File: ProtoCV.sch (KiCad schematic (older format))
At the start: 142 parts, among them J1 AudioJack2_SwitchT, J10 Conn_01x01_Male, J11 Conn_01x05_Male, J12 Conn_01x09_Male, J13 AudioJack2_SwitchT, J14 AudioJack2_SwitchT, J15 AudioJack2_SwitchT, J16 AudioJack2_SwitchT, J17 AudioJack2_SwitchT, J18 AudioJack2_SwitchT, J19 AudioJack2_SwitchT, J2 AudioJack2_SwitchT, J20 AudioJack2_SwitchT, J21 Conn_01x01_Male, J22 Conn_01x01_Male, J23 Conn_01x01_Male, J24 Conn_01x01_Male, J25 Conn_01x01_Male, J26 Conn_01x01_Male, J27 Conn_01x01_Male, J28 Conn_01x01_Male, J29 Conn_01x01_Male, J3 AudioJack2_SwitchT, J30 Conn_01x01_Male, J4 AudioJack2_SwitchT, J5 AudioJack2_SwitchT, J6 AudioJack2_SwitchT, J7 AudioJack2_SwitchT, J8 AudioJack2_SwitchT, J9 Conn_02x05_Odd_Even, Q1 BC847, Q2 BC847, Q3 BC847, Q4 BC847, Q5 BC847, Q6 BC847, Q7 BC847, Q8 BC847, U1 OPA4192, U2 OPA4192, U3 ADC80508Z, U4 R-78E3.3-0.5, U5 LD2981ABU33TR, U6 74AHCT244, U7 L7805

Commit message: Lots of manual routing.
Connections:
- net CV1: now also R12.1, R8.1; no longer R10.1, R6.1
- net CV2: now also R17.1, R21.1; no longer R11.1, R7.1
- net CV3: now also R20.1, R24.1; no longer R12.1, R8.1
- net CV4: now also R19.1, R23.1; no longer R17.1, R21.1
- net CV6: now also R11.1, R7.1; no longer R19.1, R23.1
- net CV7: now also R10.1, R6.1; no longer R20.1, R24.1
- net OUT1: now also R4.2; no longer R2.2
- net OUT2: now also R13.2; no longer R3.2
- net OUT3: now also R16.2; no longer R4.2
- net OUT4: now also R15.2; no longer R13.2
- net OUT6: now also R3.2; no longer R15.2
- net OUT7: now also R2.2; no longer R16.2
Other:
- moved on the sheet: C10, C2, C3, C4, C7, C9, R10, R11, R12, R13, R15, R16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

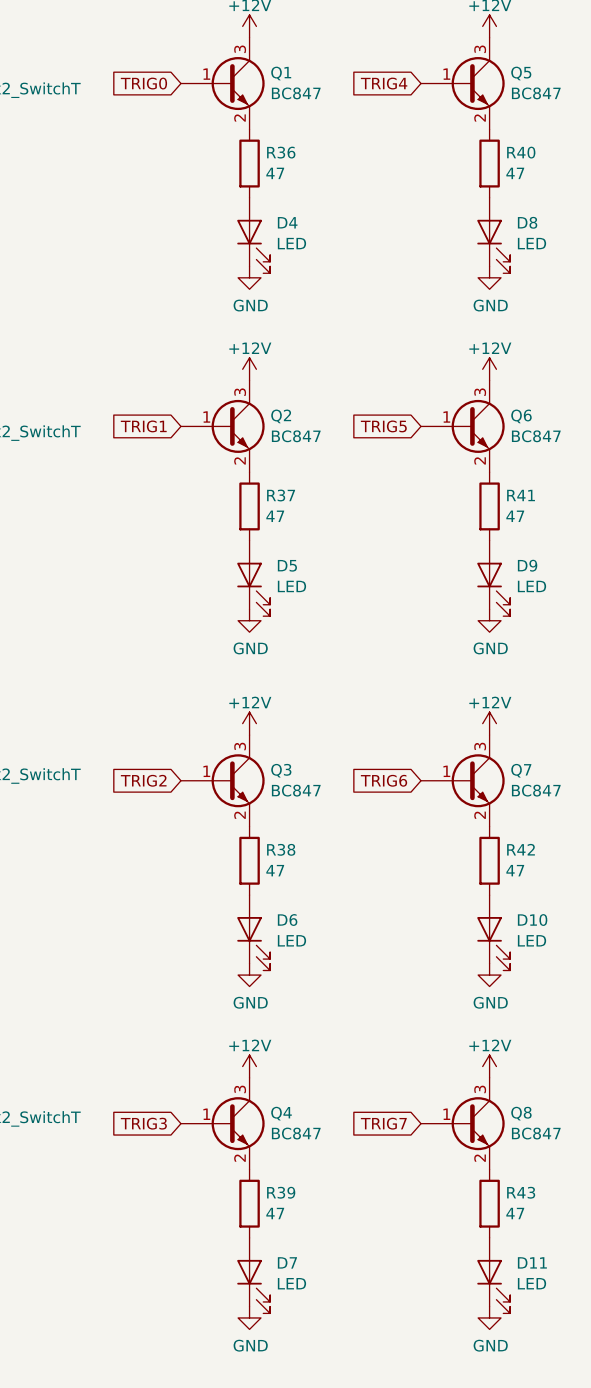
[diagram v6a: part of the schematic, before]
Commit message: Corrected led resistor values.
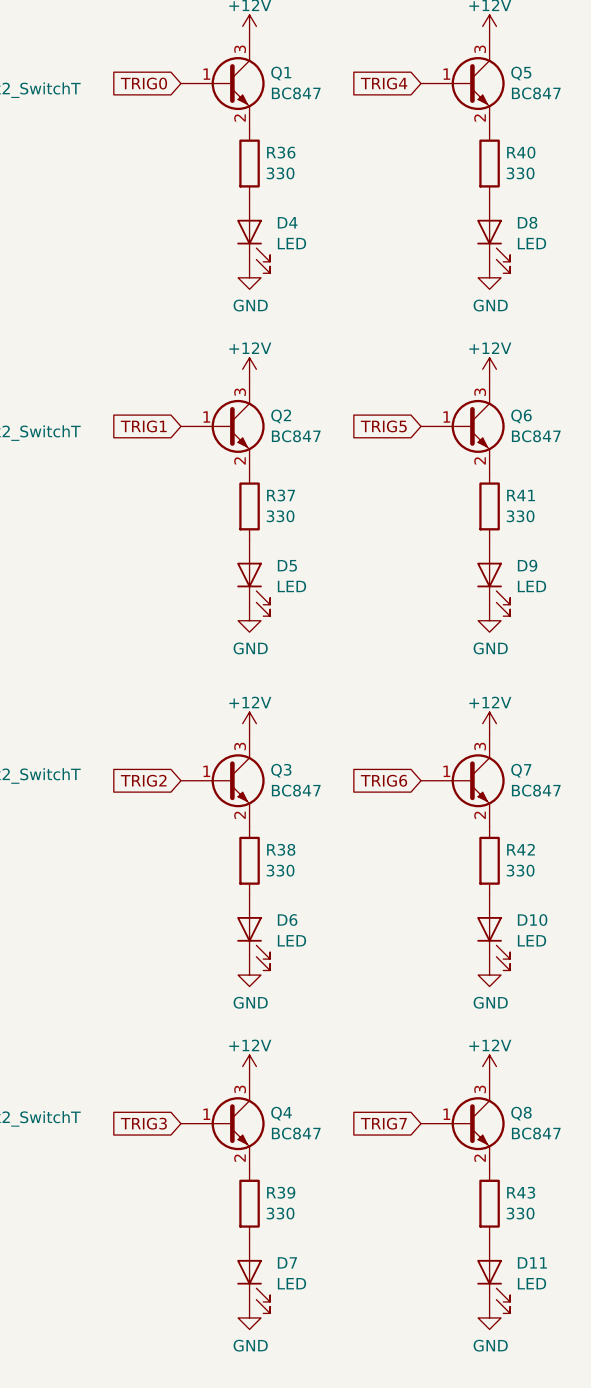
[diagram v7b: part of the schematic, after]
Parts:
- R36, R37, R38, R39, R40, R41, R42, R43: value 47 -> 330
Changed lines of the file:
@@
 P 14300 1750
 F 0 "R36" H 14370 1796 50  0000 L CNN
-F 1 "47" H 14370 1705 50  0000 L CNN
+F 1 "330" H 14370 1705 50  0000 L CNN
 F 2 "Resistor_SMD:R_0603_1608Metric" V 14230 1750 50  0001 C CNN
 F 3 "~" H 14300 1750 50  0001 C CNN
@@
 P 15350 1750
 F 0 "R40" H 15420 1796 50  0000 L CNN
-F 1 "47" H 15420 1705 50  0000 L CNN
+F 1 "330" H 15420 1705 50  0000 L CNN
 F 2 "Resistor_SMD:R_0603_1608Metric" V 15280 1750 50  0001 C CNN
 F 3 "~" H 15350 1750 50  0001 C CNN
@@
 P 14300 3250
 F 0 "R37" H 14370 3296 50  0000 L CNN
-F 1 "47" H 14370 3205 50  0000 L CNN
+F 1 "330" H 14370 3205 50  0000 L CNN
 F 2 "Resistor_SMD:R_0603_1608Metric" V 14230 3250 50  0001 C CNN
 F 3 "~" H 14300 3250 50  0001 C CNN
@@
 P 15350 3250
 F 0 "R41" H 15420 3296 50  0000 L CNN
-F 1 "47" H 15420 3205 50  0000 L CNN
+F 1 "330" H 15420 3205 50  0000 L CNN
 F 2 "Resistor_SMD:R_0603_1608Metric" V 15280 3250 50  0001 C CNN
 F 3 "~" H 15350 3250 50  0001 C CNN
@@
 P 14300 4800
 F 0 "R38" H 14370 4846 50  0000 L CNN
-F 1 "47" H 14370 4755 50  0000 L CNN
+F 1 "330" H 14370 4755 50  0000 L CNN
 F 2 "Resistor_SMD:R_0603_1608Metric" V 14230 4800 50  0001 C CNN
 F 3 "~" H 14300 4800 50  0001 C CNN
@@
 P 15350 4800
 F 0 "R42" H 15420 4846 50  0000 L CNN
-F 1 "47" H 15420 4755 50  0000 L CNN
+F 1 "330" H 15420 4755 50  0000 L CNN
 F 2 "Resistor_SMD:R_0603_1608Metric" V 15280 4800 50  0001 C CNN
 F 3 "~" H 15350 4800 50  0001 C CNN
@@
 P 14300 6300
 F 0 "R39" H 14370 6346 50  0000 L CNN
-F 1 "47" H 14370 6255 50  0000 L CNN
+F 1 "330" H 14370 6255 50  0000 L CNN
 F 2 "Resistor_SMD:R_0603_1608Metric" V 14230 6300 50  0001 C CNN
 F 3 "~" H 14300 6300 50  0001 C CNN
@@
 P 15350 6300
 F 0 "R43" H 15420 6346 50  0000 L CNN
-F 1 "47" H 15420 6255 50  0000 L CNN
+F 1 "330" H 15420 6255 50  0000 L CNN
 F 2 "Resistor_SMD:R_0603_1608Metric" V 15280 6300 50  0001 C CNN
 F 3 "~" H 15350 6300 50  0001 C CNN
